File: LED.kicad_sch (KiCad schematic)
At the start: 6 parts, among them IC1 PAM2804AAB010

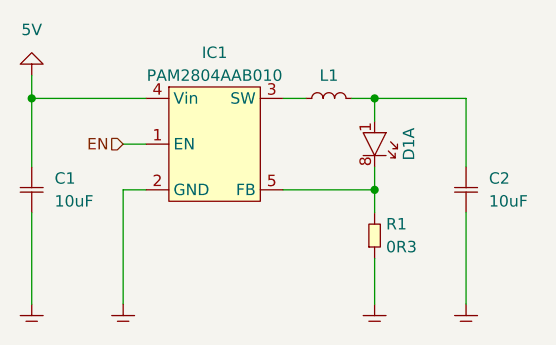
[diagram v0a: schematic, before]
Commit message: added connector, mounting holes. completed layout
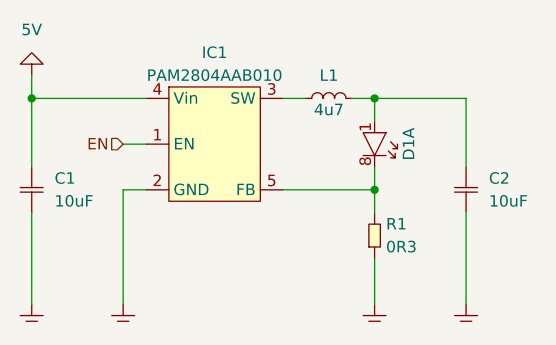
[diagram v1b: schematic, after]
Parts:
- D1: value (none) -> QLSP06RGBXWAJ; footprint (none) -> SMT:3030_8
- L1: value (none) -> 4u7; footprint (none) -> inductor:CDRH2D11
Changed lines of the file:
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@@
     (in_bom yes) (on_board yes)
     (property "Reference" "L1" (id 0) (at 157.48 83.82 0))
-    (property "Value" "" (id 1) (at 157.48 87.63 0))
-    (property "Footprint" "" (id 2) (at 157.48 86.36 0)
+    (property "Value" "4u7" (id 1) (at 157.48 87.63 0))
+    (property "Footprint" "inductor:CDRH2D11" (id 2) (at 157.48 86.36 0)
       (effects (font (size 1.27 1.27)) hide)
     )
@@
     (in_bom yes) (on_board yes)
     (property "Reference" "D1" (id 0) (at 166.37 91.44 0))
-    (property "Value" "" (id 1) (at 172.72 95.25 0)
+    (property "Value" "QLSP06RGBXWAJ" (id 1) (at 172.72 95.25 0)
       (effects (font (size 1.27 1.27)) hide)
     )
-    (property "Footprint" "" (id 2) (at 172.72 96.52 0)
+    (property "Footprint" "SMT:3030_8" (id 2) (at 172.72 96.52 0)
       (effects (font (size 1.27 1.27)) hide)
     )

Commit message: changed layout to match d1 mini
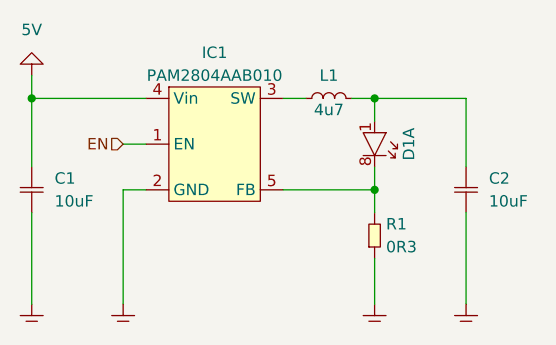
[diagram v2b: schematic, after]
